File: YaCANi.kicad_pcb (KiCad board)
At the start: 2 copper layers, 36 x 61.1 mm, 40 parts, among them P1 USB, P2 SWD, P3 DB9, U1 STM32F042C6T6, U2 AAT3221, U3 MCP2551-I/SN, X1 16 MHz

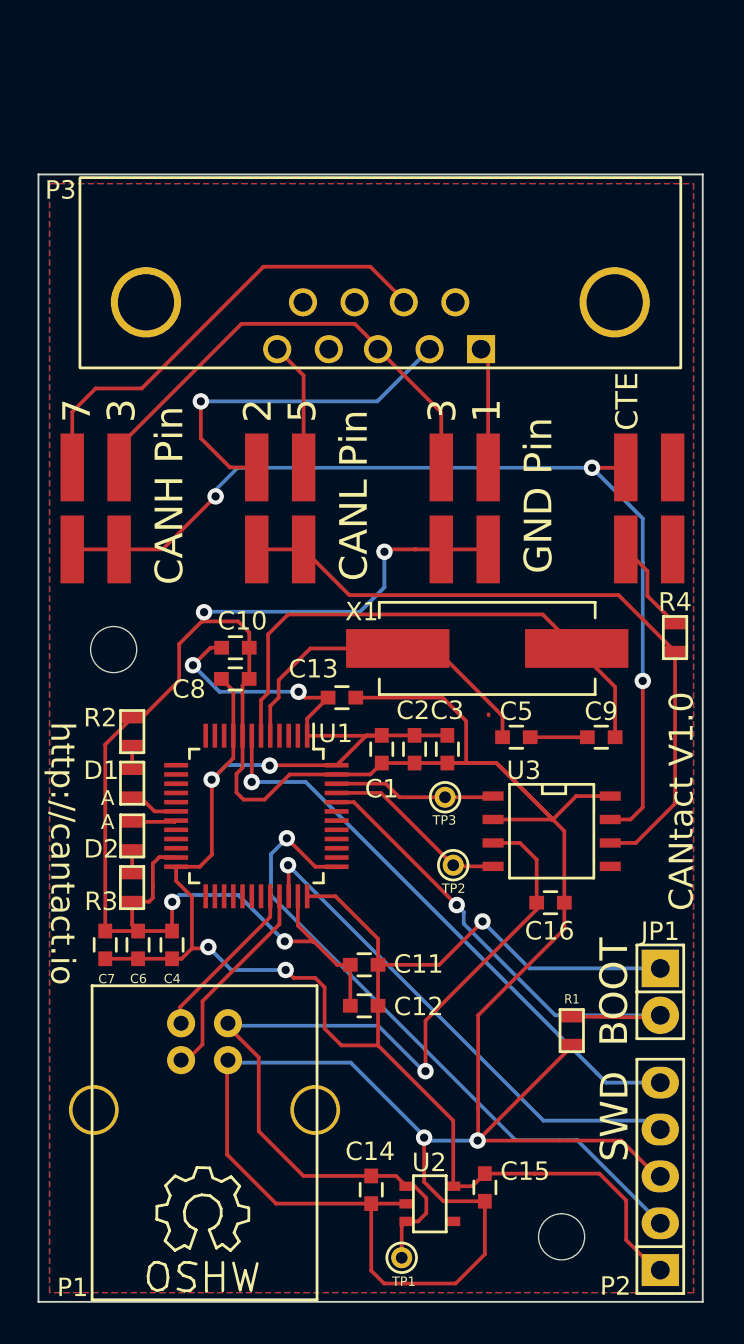
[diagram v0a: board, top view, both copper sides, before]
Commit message: updated libs, footprints
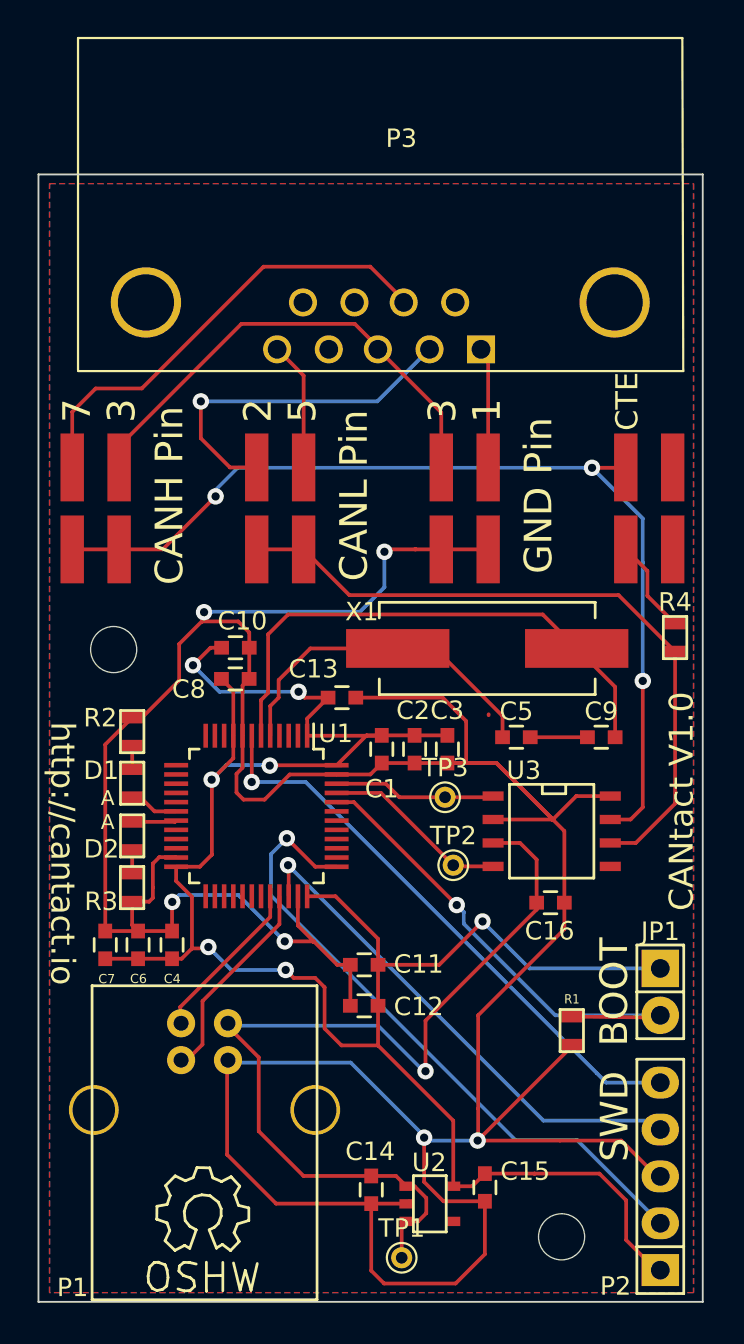
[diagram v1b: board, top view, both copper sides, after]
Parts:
- D1: value LED -> LED-GREEN
- D2: value LED -> LED-RED
- P3: footprint Connect:DB9MC -> Connectors:DB9MC
- R2, R3: value R -> 120
- TP1: value TST -> 5V; footprint Connect:PINTST -> Connectors:PINTST
- TP2: value TST -> CAN_Rx; footprint Connect:PINTST -> Connectors:PINTST
- TP3: value TST -> CAN_Tx; footprint Connect:PINTST -> Connectors:PINTST
- moved P3 5.73 mm to (148.3, 100.2)
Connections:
- net +3.3V renamed +3V3
- P1 pad 4: GND -> Net-(P1-Pad4)
- P1 pad 5: Net-(P1-Pad5) -> GND
- P1 pad 6: Net-(P1-Pad6) -> GND
- U3 pad 1: /CAN_TX -> /CAN_RX
- U3 pad 4: /CAN_RX -> /CAN_TX
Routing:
- net GND: track 212.1 -> 200.4 mm
- net Net-(P1-Pad4): track 0.00 -> 11.7 mm

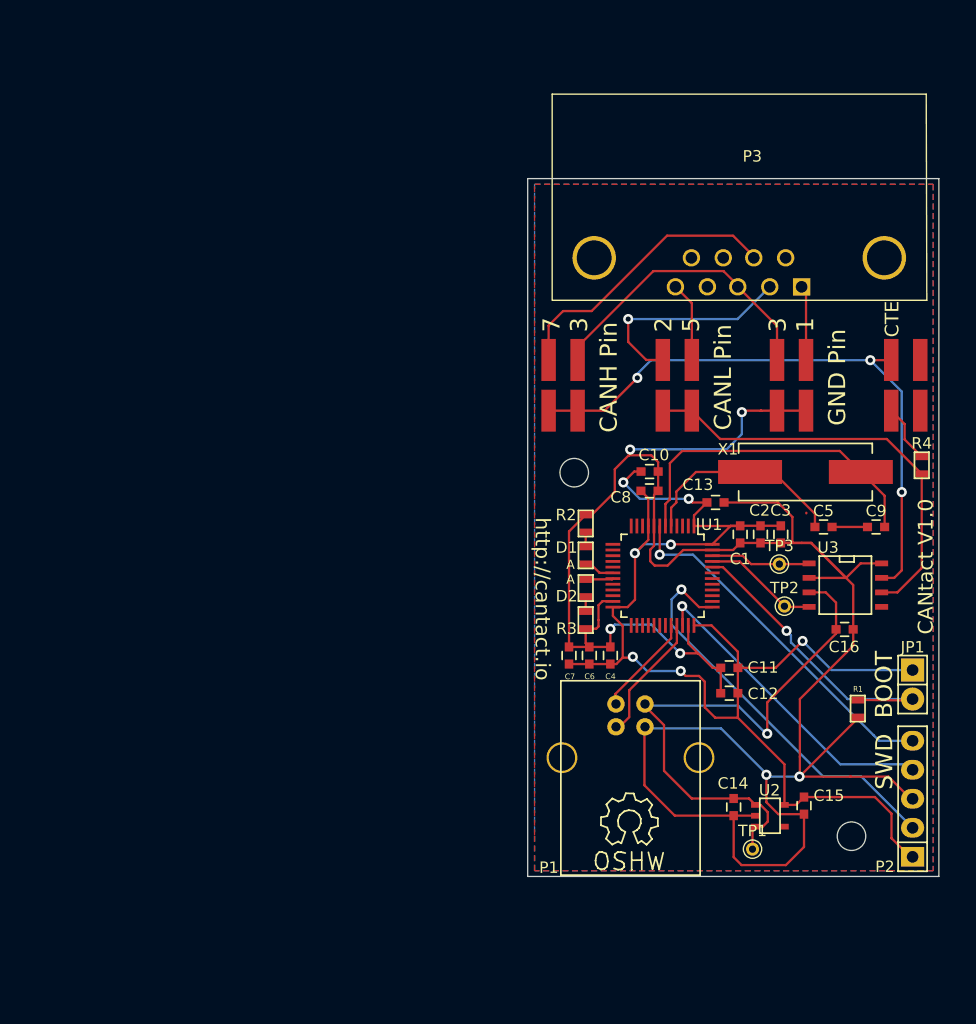
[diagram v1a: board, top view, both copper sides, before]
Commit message: new footprints on pcb
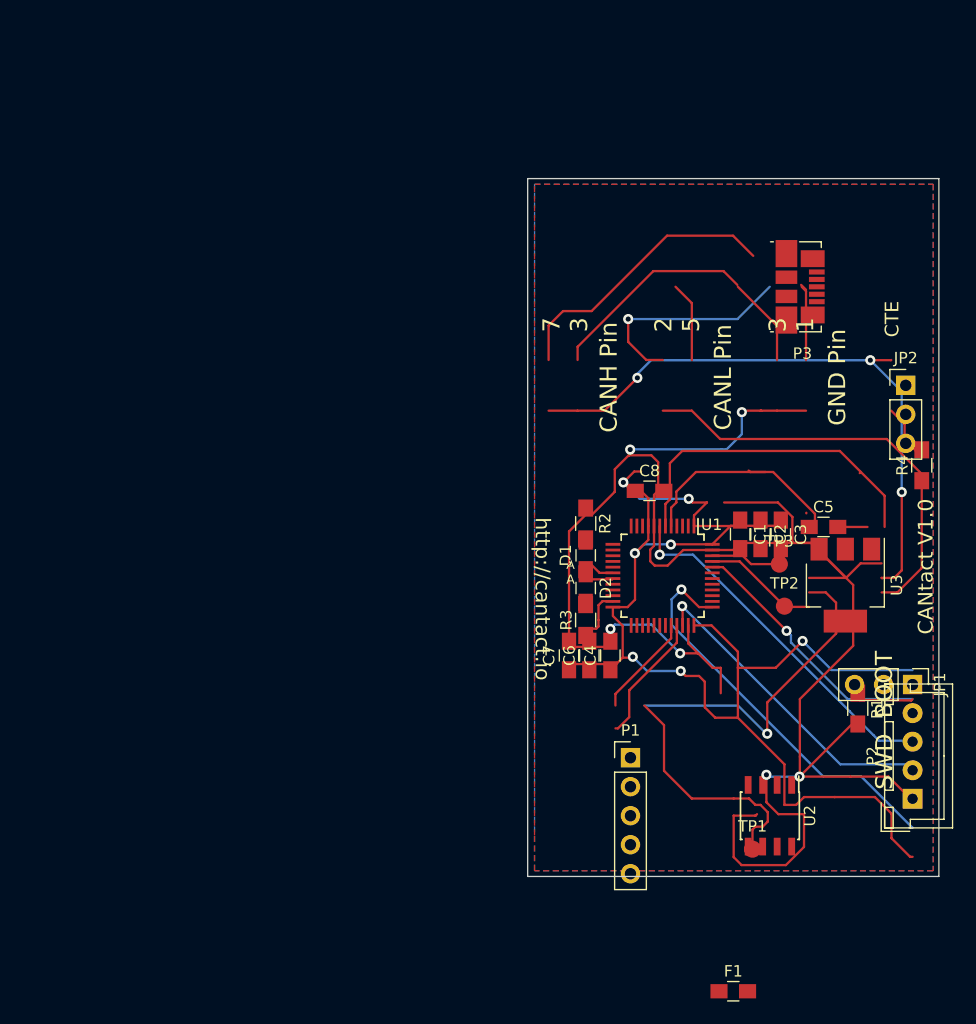
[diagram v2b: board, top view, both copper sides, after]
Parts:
- removed ? (x2): VAL**, Mounting_Holes:MountingHole_2-5mm
- removed C10, C14, C15: 1uF, Capacitors_SMD:C_0603
- removed C11, C13, C16: 0.1uF, Capacitors_SMD:C_0603
- removed C12: 4.7uF, Capacitors_SMD:C_0603
- removed C9: 18pF, Capacitors_SMD:C_0603
- removed JP3: CANH Select, cantact:0015912040
- removed JP4: CANL Select, cantact:0015912040
- removed JP5: GND Select, cantact:0015912040
- removed SYM: Symbol_OSHW-Logo_SilkScreen_07Jul2012, Symbols:Symbol_OSHW-Logo_SilkScreen
- removed X1: 16 MHz, Crystals:Crystal_HC49-SD_SMD
- added F1: Polyfuse, Capacitors_SMD:C_0805_HandSoldering, F.Cu at (142.3, 161.9)
- C1, C2, C4, C6: footprint Capacitors_SMD:C_0603 -> Capacitors_SMD:C_0805_HandSoldering
- C3: value 4.7uF -> 1uF; footprint Capacitors_SMD:C_0603 -> Capacitors_SMD:C_0805_HandSoldering
- C5: value 18pF -> 0.1uF; footprint Capacitors_SMD:C_0603 -> Capacitors_SMD:C_0805_HandSoldering
- C7: value 4.7uF -> 100nF; footprint Capacitors_SMD:C_0603 -> Capacitors_SMD:C_0805_HandSoldering
- C8: value 10nF -> 10uF; footprint Capacitors_SMD:C_0603 -> Capacitors_SMD:C_0805_HandSoldering
- D1: value LED-GREEN -> LED-RED; footprint SMD_Packages:SMD-0603 -> Capacitors_SMD:C_0805_HandSoldering
- D2: value LED-RED -> LED-GREEN; footprint SMD_Packages:SMD-0603 -> Capacitors_SMD:C_0805_HandSoldering
- JP1: value Boot Mode -> Jumper_NC_Dual; footprint Pin_Headers:Pin_Header_Straight_1x02 -> Pin_Headers:Pin_Header_Straight_1x03_Pitch2.54mm
- JP2: value Term Enable -> Jumper_NC_Dual; footprint cantact:0015912040 -> Pin_Headers:Pin_Header_Straight_1x03_Pitch2.54mm
- P1: value USB -> SWD; footprint Connect:USB_B -> Pin_Headers:Pin_Header_Straight_1x05_Pitch2.54mm
- P2: value SWD -> CAN; footprint Pin_Headers:Pin_Header_Straight_1x05 -> Connectors_JST:JST_XH_B04B-XH-A_04x2.50mm_Straight
- P3: value DB9 -> USB; footprint Connectors:DB9MC -> Connectors_Molex:USB_Micro-B_Molex_47346-0001
- R1: value 510 -> 120; footprint SMD_Packages:SMD-0603 -> Resistors_SMD:R_0805_HandSoldering
- R2: value 120 -> 10k; footprint SMD_Packages:SMD-0603 -> Resistors_SMD:R_0805_HandSoldering
- R3, R4: value 120 -> R; footprint SMD_Packages:SMD-0603 -> Resistors_SMD:R_0805_HandSoldering
- TP1, TP2, TP3: footprint Connectors:PINTST -> Measurement_Points:Measurement_Point_Round-SMD-Pad_Small
- U2: value AAT3221 -> MCP2562-E/SN; footprint SMD_Packages:SOT-23-5 -> Housings_SOIC:SOIC-8_3.9x4.9mm_Pitch1.27mm
- U3: value MCP2551-I/SN -> LD1117S33TR; footprint SMD_Packages:SOIC-8-N -> TO_SOT_Packages_SMD:SOT-223
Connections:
- C5 pad 1: Net-(C5-Pad1) -> GND
- C5 pad 2: GND -> +5V
- C6 pad 1: +3V3 -> GND
- C6 pad 2: GND -> +3V3
- C7 pad 1: +3V3 -> (no net)
- C8 pad 1: +3V3 -> (no net)
- D1 pad 1: Net-(D1-Pad1) -> GND
- D2 pad 1: Net-(D2-Pad1) -> GND
- JP1 pad 2: Net-(JP1-Pad2) -> BOOT0
- JP2 pad 1: Net-(JP2-Pad1) -> (no net)
- JP2 pad 3: Net-(JP2-Pad3) -> CAN_L
- P1 pad 1: +5V -> +3V3
- P1 pad 2: /USB_DM -> /SWCLK
- P1 pad 3: /USB_DP -> GND
- P1 pad 4: Net-(P1-Pad4) -> /SWDIO
- P1 pad 5: GND -> /NRST
- P2 pad 1: +3V3 -> GND
- P2 pad 2: /SWCLK -> CAN_H
- P2 pad 3: GND -> CAN_L
- P2 pad 4: /SWDIO -> (no net)
- P3 pad 1: /DB9_1 -> Net-(F1-Pad1)
- P3 pad 2: /DB9_2 -> /USB_DM
- P3 pad 3: /DB9_3 -> /USB_DP
- P3 pad 4: Net-(P3-Pad4) -> (no net)
- P3 pad 5: /DB9_5 -> GND
- P3 pad 6: Net-(P3-Pad6) -> GND
- R1 pad 1: Net-(JP1-Pad2) -> Net-(JP2-Pad2)
- R1 pad 2: GND -> CAN_H
- R2 pad 1: GND -> BOOT0
- R2 pad 2: Net-(D1-Pad2) -> GND
- R3 pad 1: GND -> Net-(D1-Pad2)
- R3 pad 2: Net-(D2-Pad2) -> LED_ACT
- R4 pad 1: Net-(JP4-Pad1) -> Net-(D2-Pad2)
- R4 pad 2: Net-(JP2-Pad1) -> LED_PWR
- U1 pad 10: Net-(U1-Pad10) -> (no net)
- U1 pad 11: Net-(U1-Pad11) -> (no net)
- U1 pad 12: Net-(U1-Pad12) -> (no net)
- U1 pad 13: Net-(U1-Pad13) -> (no net)
- U1 pad 14: Net-(U1-Pad14) -> (no net)
- U1 pad 15: Net-(U1-Pad15) -> (no net)
- U1 pad 16: Net-(U1-Pad16) -> (no net)
- U1 pad 17: Net-(U1-Pad17) -> (no net)
- U1 pad 18: Net-(D1-Pad1) -> LED_PWR
- U1 pad 19: Net-(D2-Pad1) -> LED_ACT
- U1 pad 2: Net-(U1-Pad2) -> (no net)
- U1 pad 20: Net-(U1-Pad20) -> (no net)
- U1 pad 21: Net-(U1-Pad21) -> (no net)
- U1 pad 22: Net-(U1-Pad22) -> (no net)
- U1 pad 25: Net-(U1-Pad25) -> (no net)
- U1 pad 26: Net-(U1-Pad26) -> (no net)
- U1 pad 27: Net-(U1-Pad27) -> (no net)
- U1 pad 28: Net-(U1-Pad28) -> (no net)
- U1 pad 29: Net-(U1-Pad29) -> (no net)
- U1 pad 3: Net-(U1-Pad3) -> (no net)
- U1 pad 30: Net-(U1-Pad30) -> (no net)
- U1 pad 31: Net-(U1-Pad31) -> (no net)
- U1 pad 38: Net-(U1-Pad38) -> (no net)
- U1 pad 39: Net-(U1-Pad39) -> (no net)
- U1 pad 4: Net-(U1-Pad4) -> (no net)
- U1 pad 40: Net-(U1-Pad40) -> (no net)
- U1 pad 41: Net-(U1-Pad41) -> (no net)
- U1 pad 42: Net-(U1-Pad42) -> (no net)
- U1 pad 43: Net-(U1-Pad43) -> (no net)
- U1 pad 44: Net-(JP1-Pad2) -> BOOT0
- U1 pad 5: Net-(C5-Pad1) -> (no net)
- U1 pad 6: Net-(C9-Pad1) -> (no net)
- U2 pad 1: +5V -> /CAN_RX
- U2 pad 4: (no net) -> /CAN_TX
- U3 pad 1: /CAN_RX -> GND
- U3 pad 2: GND -> +3V3
- U3 pad 4: /CAN_TX -> (no net)
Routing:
- net (no net): track 0.05 -> 135.0 mm, vias 0 -> 2
- net Net-(JP4-Pad1): track 37.6 -> 0.00 mm
- net Net-(D2-Pad2): track 1.28 -> 37.6 mm
- net Net-(C9-Pad1): track 29.4 -> 0.00 mm
- net BOOT0: track 0.00 -> 28.1 mm, vias 0 -> 1
- net Net-(JP1-Pad2): track 27.5 -> 0.00 mm, vias 1 -> 0
- net /DB9_3: track 26.2 -> 0.00 mm
- net /DB9_7: track 24.9 -> 0.00 mm
- net Net-(C5-Pad1): track 20.3 -> 0.00 mm
- net /DB9_2: track 19.3 -> 0.00 mm, vias 1 -> 0
- net GND: track 200.4 -> 181.8 mm
- net CAN_H: track 0.00 -> 13.8 mm
- net Net-(P1-Pad4): track 11.7 -> 0.00 mm
- net CAN_L: track 0.00 -> 8.05 mm
- net /DB9_1: track 7.18 -> 0.00 mm
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
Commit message: first placement and quick routing
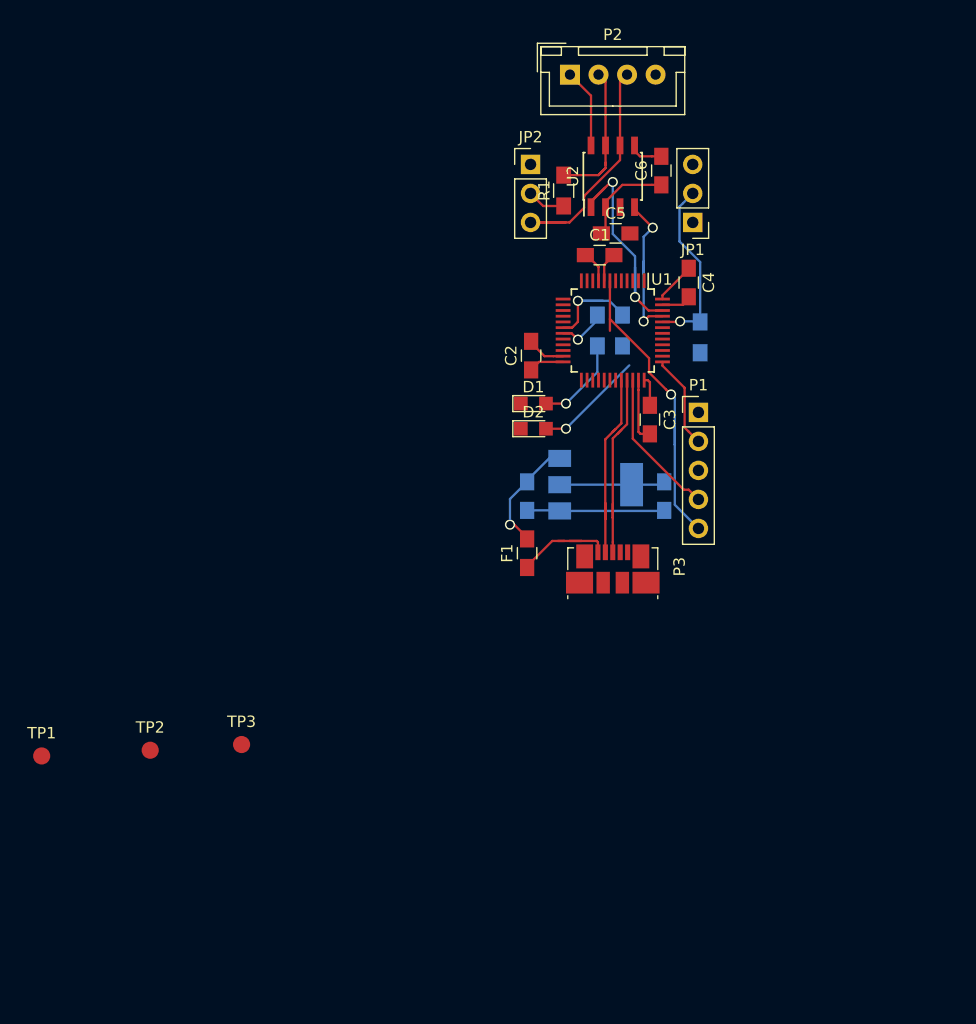
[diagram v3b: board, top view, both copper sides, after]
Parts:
- C7, C8, R2, R3, R4, U3: moved to B.Cu
- D1, D2: footprint Capacitors_SMD:C_0805_HandSoldering -> LEDs:LED_0805
- moved P2 70.1 mm to (128.0, 81.6), turned to 0 degrees
- moved TP1 62.8 mm to (81.8, 141.2)
- moved U2 57.7 mm to (131.8, 90.5), turned to 90 degrees
- moved TP2 56.9 mm to (91.2, 140.8)
- moved R1 52.2 mm to (127.5, 91.8), turned to 90 degrees
- moved TP3 49.7 mm to (99.2, 140.2)
- moved JP1 44.8 mm to (138.8, 94.5), turned to 180 degrees
- moved C6 42.9 mm to (136.0, 90.0)
- moved F1 42.4 mm to (124.2, 123.5), turned to 90 degrees
- moved JP2 38.1 mm to (124.5, 89.5)
- moved C4 33.4 mm to (138.4, 99.8), turned to 270 degrees
- moved C5 31.5 mm to (132.0, 95.5)
- moved P1 30.8 mm to (139.2, 111.2)
- moved P3 29.6 mm to (131.8, 124.8), turned to 90 degrees
- moved R4 28.7 mm to (132.6, 104.0)
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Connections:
- C7 pad 1: (no net) -> +5V
- C8 pad 1: (no net) -> +3V3
- U2 pad 1: /CAN_RX -> /CAN_TX
- U2 pad 4: /CAN_TX -> /CAN_RX
- U2 pad 6: CAN_H -> CAN_L
- U2 pad 7: CAN_L -> CAN_H
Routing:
- net GND: track 181.8 -> 41.5 mm, vias 6 -> 0
- net (no net): track 135.0 -> 0.00 mm, vias 2 -> 0
- net +3V3: track 116.9 -> 24.3 mm, vias 7 -> 0
- net Net-(JP2-Pad2): track 58.6 -> 3.36 mm, vias 3 -> 0
- net +5V: track 45.5 -> 10.2 mm, vias 0 -> 1
- net Net-(D2-Pad2): track 37.6 -> 9.60 mm, vias 0 -> 1
- net /SWCLK: track 35.6 -> 8.26 mm, vias 1 -> 0
- net /CAN_TX: track 5.14 -> 21.2 mm, vias 0 -> 2
- net CAN_L: track 8.05 -> 21.5 mm
- net BOOT0: track 28.1 -> 15.8 mm
- net Net-(F1-Pad1): track 0.00 -> 9.77 mm
- net LED_PWR: track 1.17 -> 10.0 mm, vias 0 -> 1
- net /USB_DM: track 9.04 -> 17.4 mm
- net /SWDIO: track 21.3 -> 13.1 mm, vias 1 -> 0
- net /USB_DP: track 11.4 -> 17.2 mm
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- removed copper zone on B.Cu, net GND
- removed copper zone on F.Cu, net GND
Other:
- board outline removed
- board text removed: "2 5"
- board text removed: "3 1"
- board text removed: "7 3"
- board text removed: "A"
- board text removed: "BOOT"
- board text removed: "CANH Pin"
- board text removed: "CANL Pin"
- board text removed: "CANtact V1.0"
- board text removed: "CTE"
- board text removed: "GND Pin"
- board text removed: "SWD"
- board text removed: "http://cantact.io"
